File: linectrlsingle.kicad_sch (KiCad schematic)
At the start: 32 parts, among them J3 6P4C, J4 6P4C, K1 Relay_SPST-NO, K2 Relay_SPDT, Q1 PMOS, Q2 PMOS, T1 Transformer_1P_1S

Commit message: start work on v2.1
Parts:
- R15: value 500 -> 600
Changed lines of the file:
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@@
 	(title_block
 		(title "M5 PBX Sniffer")
-		(date "2026-06-01")
-		(rev "V2")
+		(date "2026-08-17")
+		(rev "V2.1")
 		(comment 4 "Tobe Cynar")
 	)
@@
 			)
 		)
-		(property "Value" "500"
+		(property "Value" "600"
 			(at 179.07 80.0099 0)
 			(show_name no)

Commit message: unsplit grounds, finish power circuitry, start picking footprints/partnumbers
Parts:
- C1, C2: footprint Capacitor_THT:C_Rect_L7.0mm_W2.0mm_P5.00mm -> Capacitor_SMD:C_0805_2012Metric
- C3: value 0.47u -> 1u; footprint Capacitor_THT:C_Rect_L7.0mm_W2.0mm_P5.00mm -> Capacitor_SMD:C_0805_2012Metric
- D1, D2, D3, D4: value 1N4148 -> BAT54LT1G; footprint Diode_THT:D_DO-35_SOD27_P7.62mm_Horizontal -> Package_TO_SOT_SMD:SOT-23; DKPN (none) -> BAT54LT1GOSCT-ND
- R10, R11, R12, R13, R14, R15, R16, R9: footprint Resistor_THT:R_Axial_DIN0207_L6.3mm_D2.5mm_P7.62mm_Horizontal -> Resistor_SMD:R_0805_2012Metric
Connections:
- net GNDD is gone; now on net GND: D3.2 (A), D4.2 (A), J4.SH, K1.1, K2.5

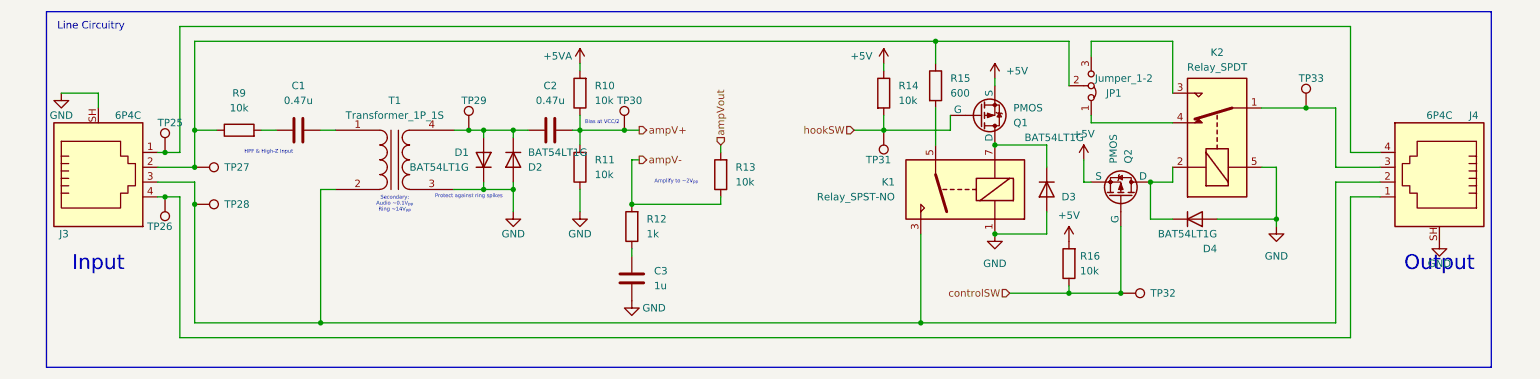
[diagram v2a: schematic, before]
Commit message: added power mux, finished up schematic and picking footprints/partnumbers
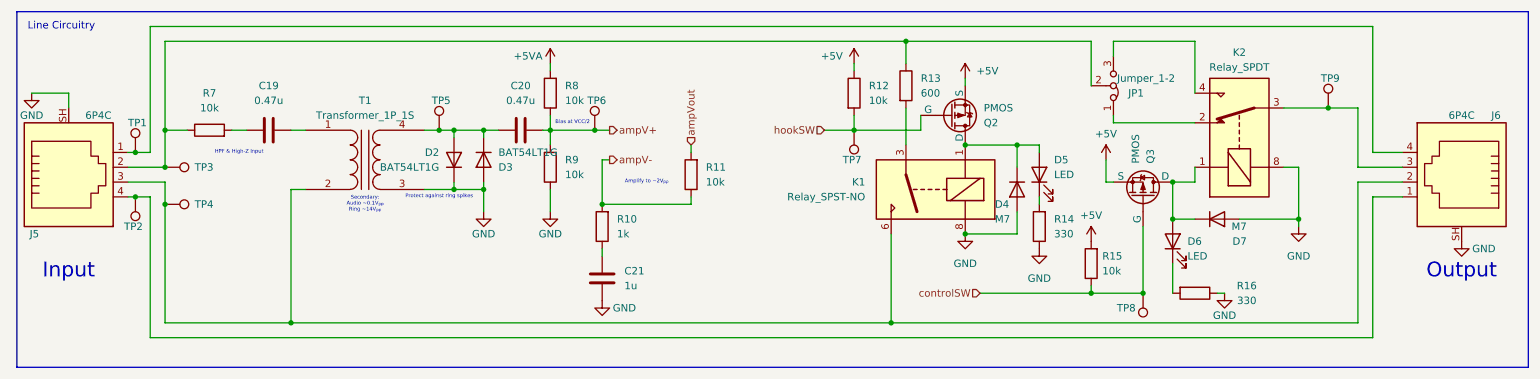
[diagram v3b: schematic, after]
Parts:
- added D5, D6: LED, Resistor_SMD:R_0603_1608Metric, symbol Device:LED
- added R14, R16: 330, Resistor_SMD:R_0805_2012Metric, symbol Device:R
- D4: renamed from D3; value BAT54LT1G -> M7; footprint Package_TO_SOT_SMD:SOT-23 -> Diode_SMD:D_SMA; DKPN BAT54LT1GOSCT-ND -> 4878-M7CT-ND
- D7: renamed from D4; value BAT54LT1G -> M7; footprint Package_TO_SOT_SMD:SOT-23 -> Diode_SMD:D_SMA; DKPN BAT54LT1GOSCT-ND -> 4878-M7CT-ND
- K1: footprint Relay_THT:Relay_SPST_StandexMeder_SIL_Form1A -> Relay_SMD:Relay_2P2T_10x6mm_TE_IMxxG; DKPN 1835-1116-ND -> 41-IMB03IGRCT-ND
- K2: footprint Phones:K_AZ943-1C_AMZ -> Relay_SMD:Relay_2P2T_10x6mm_TE_IMxxG; DKPN 3385-AZ943-1CH-5DE-ND -> PB1061CT-ND
- T1: DKPN 237-1121-ND -> SM-LP-5001-ND
- renumbered C1 to C19, C2 to C20, C3 to C21, D1 to D2, D2 to D3, J3 to J5, J4 to J6, Q1 to Q2, Q2 to Q3, R12 to R10, R13 to R11, R14 to R12, R15 to R13, R16 to R15, R9 to R7, R10 to R8, R11 to R9, TP25 to TP1, TP26 to TP2, TP27 to TP3, TP28 to TP4, TP29 to TP5, TP30 to TP6, TP31 to TP7, TP32 to TP8, TP33 to TP9
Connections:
- net GND: now also K1.8, K2.8, R14.1, R16.1; no longer K1.1, K2.5
- net at JP1.1 (A): now also K2.2; no longer K2.4
- net at JP1.3 (B): now also K2.4; no longer K2.3
- net at J5.3, J6.2, T1.2 (AB)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: now also K1.6; no longer K1.3
- net at D4.1 (K), Q2.1 (D): now also K1.1, D5.2 (A); no longer K1.7
- net at D7.1 (K), Q3.1 (D): now also K2.1, D6.2 (A); no longer K2.2
- net at R13.2: now also K1.3; no longer K1.5
- net at J6.3, TP9.1: now also K2.3; no longer K2.1
- new net: D5.1 (K), R14.2
- new net: D6.1 (K), R16.2
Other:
- moved on the sheet: C19, C20, C21, D2, D3, D4, D7, J5, J6, JP1, K1, K2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

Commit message: fix final footprint picking issues
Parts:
- Q2, Q3: footprint Package_TO_SOT_THT:TO-92_HandSolder -> Package_TO_SOT_SMD:SOT-23; DKPN ZVP3306A-ND -> BSS84PH6327XTSA2CT-ND
- T1: footprint Phones:TY-145P -> Phones:TRAN6_SM-LP-5001_BRN
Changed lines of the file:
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@@
 			)
 		)
-		(property "Footprint" "Package_TO_SOT_THT:TO-92_HandSolder"
+		(property "Footprint" "Package_TO_SOT_SMD:SOT-23"
 			(at 184.15 86.36 0)
 			(hide yes)
@@
 			)
 		)
-		(property "DKPN" "ZVP3306A-ND"
+		(property "DKPN" "BSS84PH6327XTSA2CT-ND"
 			(at 179.07 83.82 0)
 			(hide yes)
@@
 			)
 		)
-		(property "Footprint" "Package_TO_SOT_THT:TO-92_HandSolder"
+		(property "Footprint" "Package_TO_SOT_SMD:SOT-23"
 			(at 214.63 92.71 0)
 			(hide yes)
@@
 			)
 		)
-		(property "DKPN" "ZVP3306A-ND"
+		(property "DKPN" "BSS84PH6327XTSA2CT-ND"
 			(at 212.09 97.79 0)
 			(hide yes)
@@
 			)
 		)
-		(property "Footprint" "Phones:TY-145P"
+		(property "Footprint" "Phones:TRAN6_SM-LP-5001_BRN"
 			(at 78.74 91.44 0)
 			(hide yes)
